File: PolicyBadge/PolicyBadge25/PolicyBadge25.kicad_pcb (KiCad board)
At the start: 2 copper layers, 90.4 x 89.6 mm, 68 parts, among them CN1 PH2.0-2P-LT, J1 Feed Point 915MHz, J2 Feed Point 2.4 GHz, Q1 2N7002, SW1 TA-3525-A1, U1 HS96L03W2C03, U10 YX-SMD5020, U11 IP2312-4V35, U2 MOUDLE-SEEEDUINO-XIAO-ESP32S3, U4 TPS613222ADBVR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

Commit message: Updated PCB routing
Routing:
- net VCC_3V3: track 265.5 -> 284.2 mm
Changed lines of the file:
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@@
-	)
-	(segment
-		(start 119 56.7)
-		(end 139.1 56.7)
-		(width 0.508)
-		(layer "B.Cu")
-		(net 8)
 	)
 	(segment
@@
 	)
 	(segment
+		(start 121.4 69.5)
+		(end 118.9 67)
+		(width 0.508)
+		(layer "B.Cu")
+		(net 8)
+	)
+	(segment
 		(start 150.1 109.7)
 		(end 150.1 104.6)
@@
 	)
 	(segment
-		(start 139.1 56.7)
-		(end 142.2 53.6)
+		(start 142.2 53.1)
+		(end 142.2 66.4)
 		(width 0.508)
 		(layer "B.Cu")
@@
 	)
 	(segment
+		(start 118.9 67)
+		(end 118.9 62.2)
+		(width 0.508)
+		(layer "B.Cu")
+		(net 8)
+	)
+	(segment
 		(start 129.33 76.53)
 		(end 132.5 79.7)
@@
 	)
 	(segment
+		(start 139.1 69.5)
+		(end 121.4 69.5)
+		(width 0.508)
+		(layer "B.Cu")
+		(net 8)
+	)
+	(segment
 		(start 129.33 73.89)
 		(end 129.33 76.53)
@@
 	)
 	(segment
-		(start 142.2 53.6)
-		(end 142.2 53.1)
-		(width 0.508)
-		(layer "B.Cu")
-		(net 8)
-	)
-	(segment
 		(start 158.2 102.4)
 		(end 155.5 102.4)
 		(width 0.254)
+		(layer "B.Cu")
+		(net 8)
+	)
+	(segment
+		(start 142.2 66.4)
+		(end 139.1 69.5)
+		(width 0.508)
 		(layer "B.Cu")
 		(net 8)
@@
 		(min_thickness 0.25)
 		(filled_areas_thickness no)
-		(fill yes
+		(fill
 			(thermal_gap 0.5)
 			(thermal_bridge_width 0.5)
@@
 		(min_thickness 0.25)
 		(filled_areas_thickness no)
-		(fill yes
+		(fill
 			(thermal_gap 0.5)
 			(thermal_bridge_width 0.5)
@@
 		(min_thickness 0.25)
 		(filled_areas_thickness no)
-		(fill yes
+		(fill
 			(thermal_gap 0.5)
 			(thermal_bridge_width 0.5)
@@
 		(min_thickness 0.25)
 		(filled_areas_thickness no)
-		(fill yes
+		(fill
 			(thermal_gap 0.5)
 			(thermal_bridge_width 0.5)
@@
 		(min_thickness 0.25)
 		(filled_areas_thickness no)
-		(fill yes
+		(fill
 			(thermal_gap 0.5)
 			(thermal_bridge_width 0.5)
@@
 		(min_thickness 0.25)
 		(filled_areas_thickness no)
-		(fill yes
+		(fill
 			(thermal_gap 0.5)
 			(thermal_bridge_width 0.5)

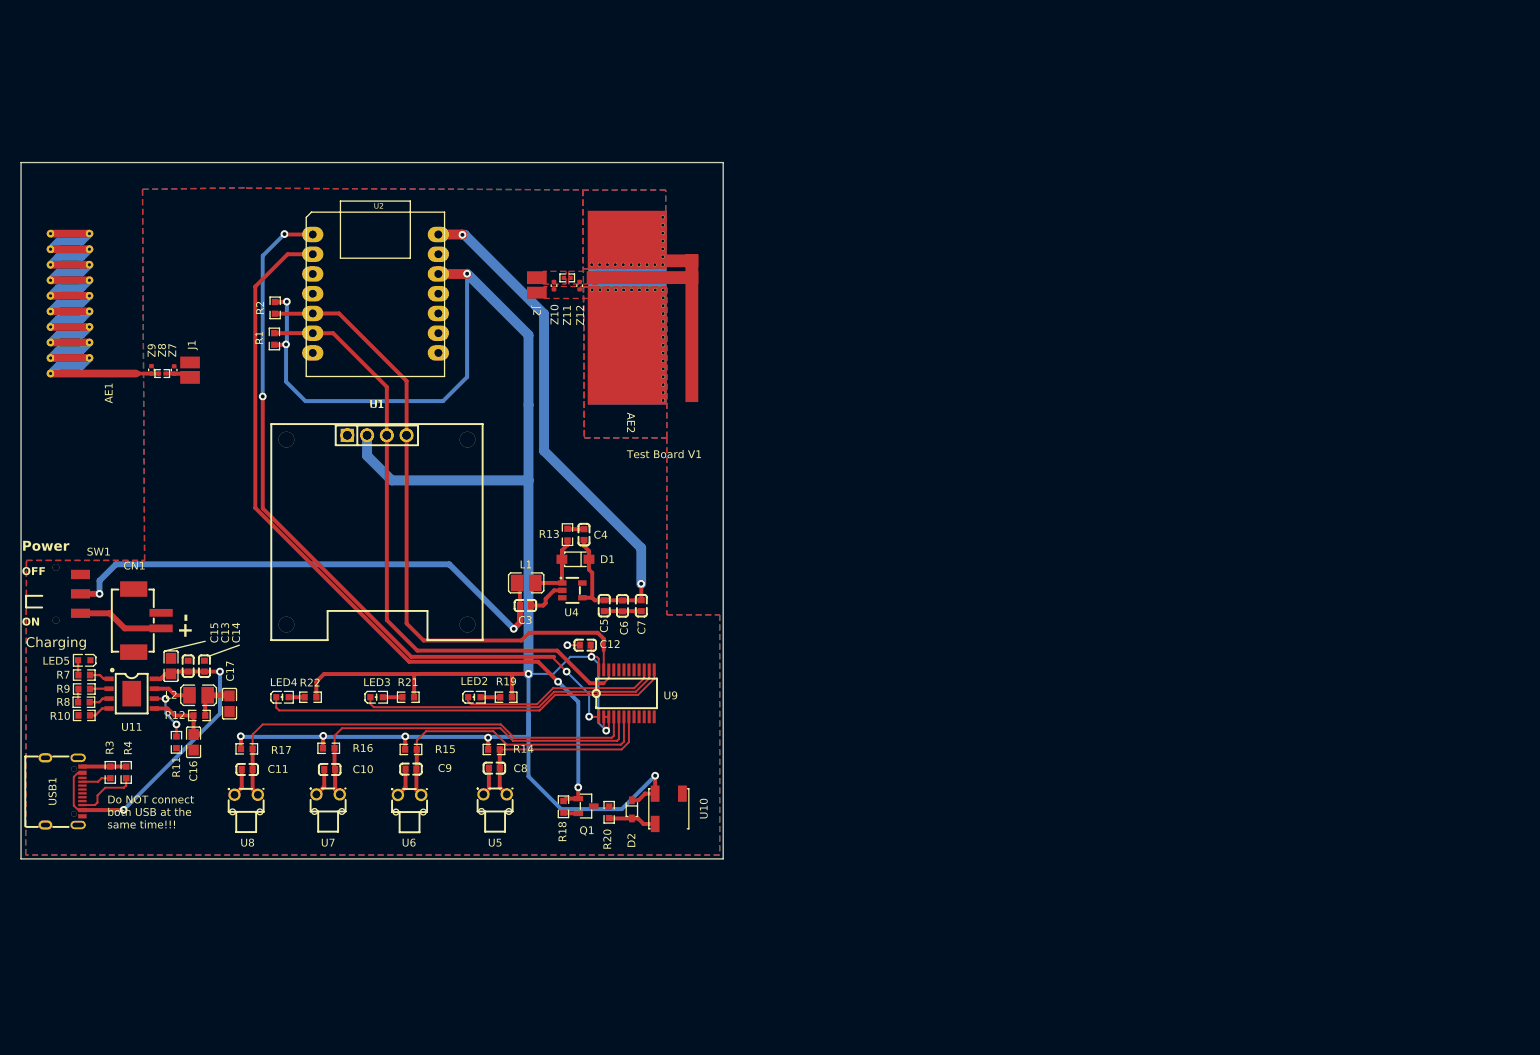
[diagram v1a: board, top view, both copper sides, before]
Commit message: minor updates
imported new switch footprint and schematic symbol. sync'ed the PCB to add R23, R5, R6. annotated.
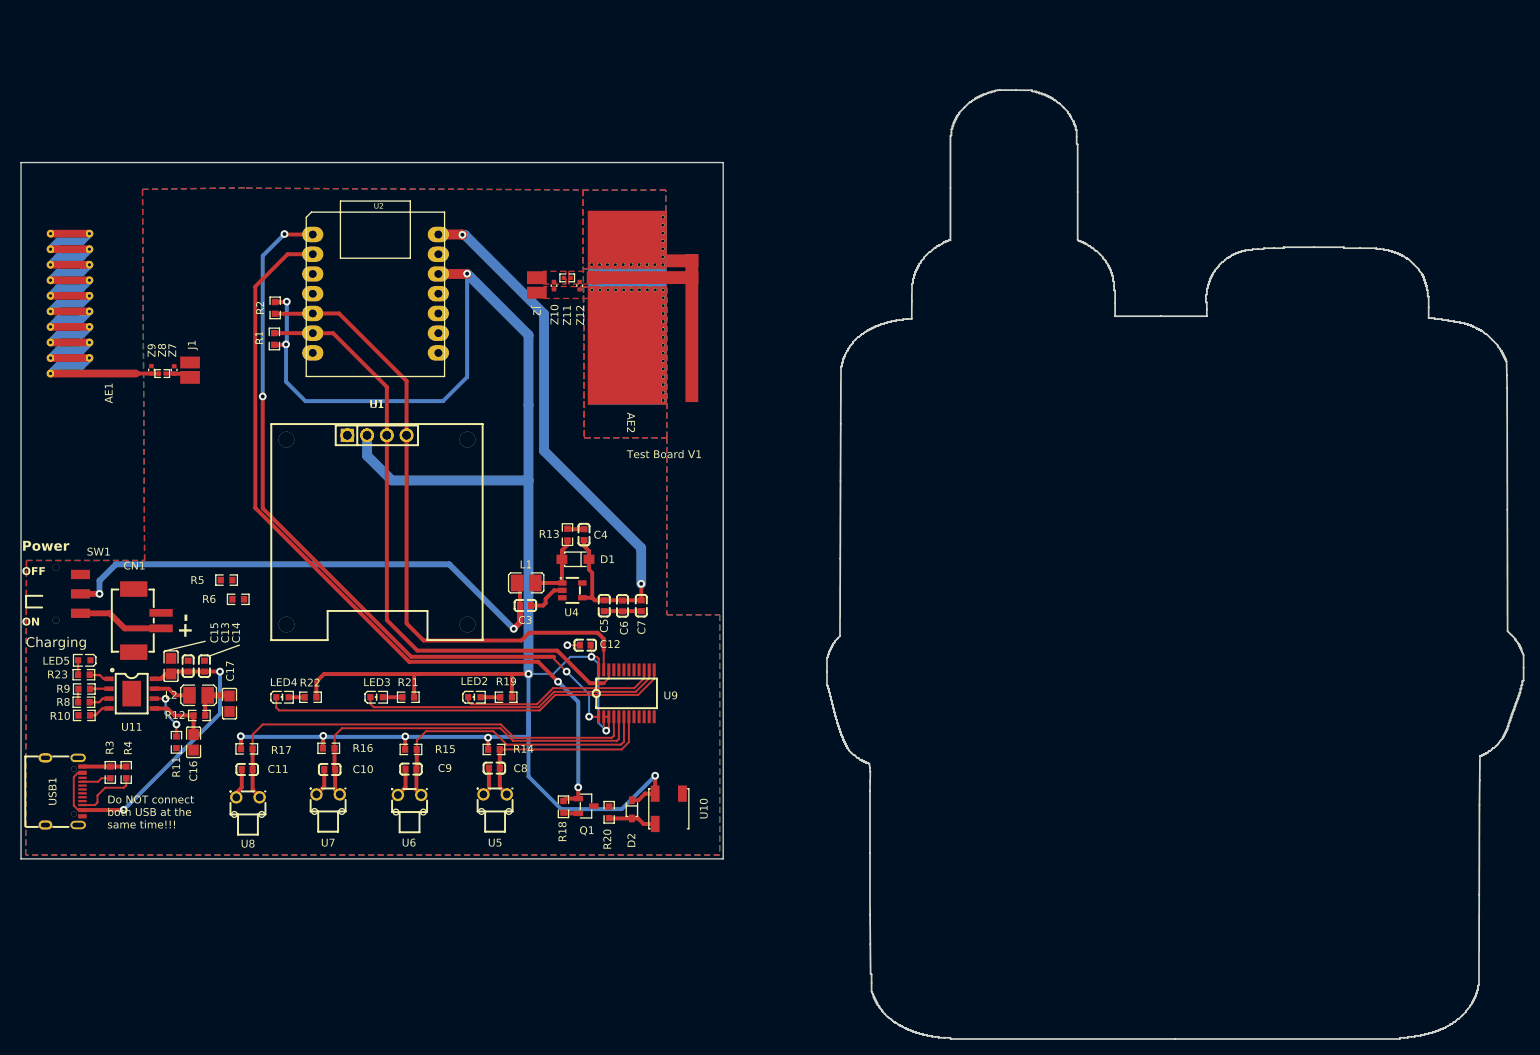
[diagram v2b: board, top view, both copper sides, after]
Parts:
- removed R7: 240Ω, imported:R0603
- added R23: 1KΩ, imported:R0603, F.Cu at (92.9, 104.7)
- added R5: 220kΩ, imported:R0603, F.Cu at (111.2, 92.5)
- added R6: 220kΩ, imported:R0603, F.Cu at (112.8, 95.0)
- moved U8 0.40 mm to (114.0, 120.5)
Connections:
- net /VBATT+ renamed VBATT+
- U2 pad 1: /IO Expander and LED's/IO_INT -> Net-(U2-PA02_A0_D0)
- U2 pad 2: /IO Expander and LED's/BUZZER -> /IO Expander and LED's/IO_INT
- U2 pad 3: unconnected-(U2-PA10_A2_D2-Pad3) -> /IO Expander and LED's/BUZZER
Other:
- board size 90.4 x 89.6 mm -> 193.3 x 122.1 mm

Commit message: battery silk screen + Lanyard
added battery silk screen outline (23mmx34mm is battery, silk screen rectangle is 25x36mm). also added edge cuts for the lanyard holes.
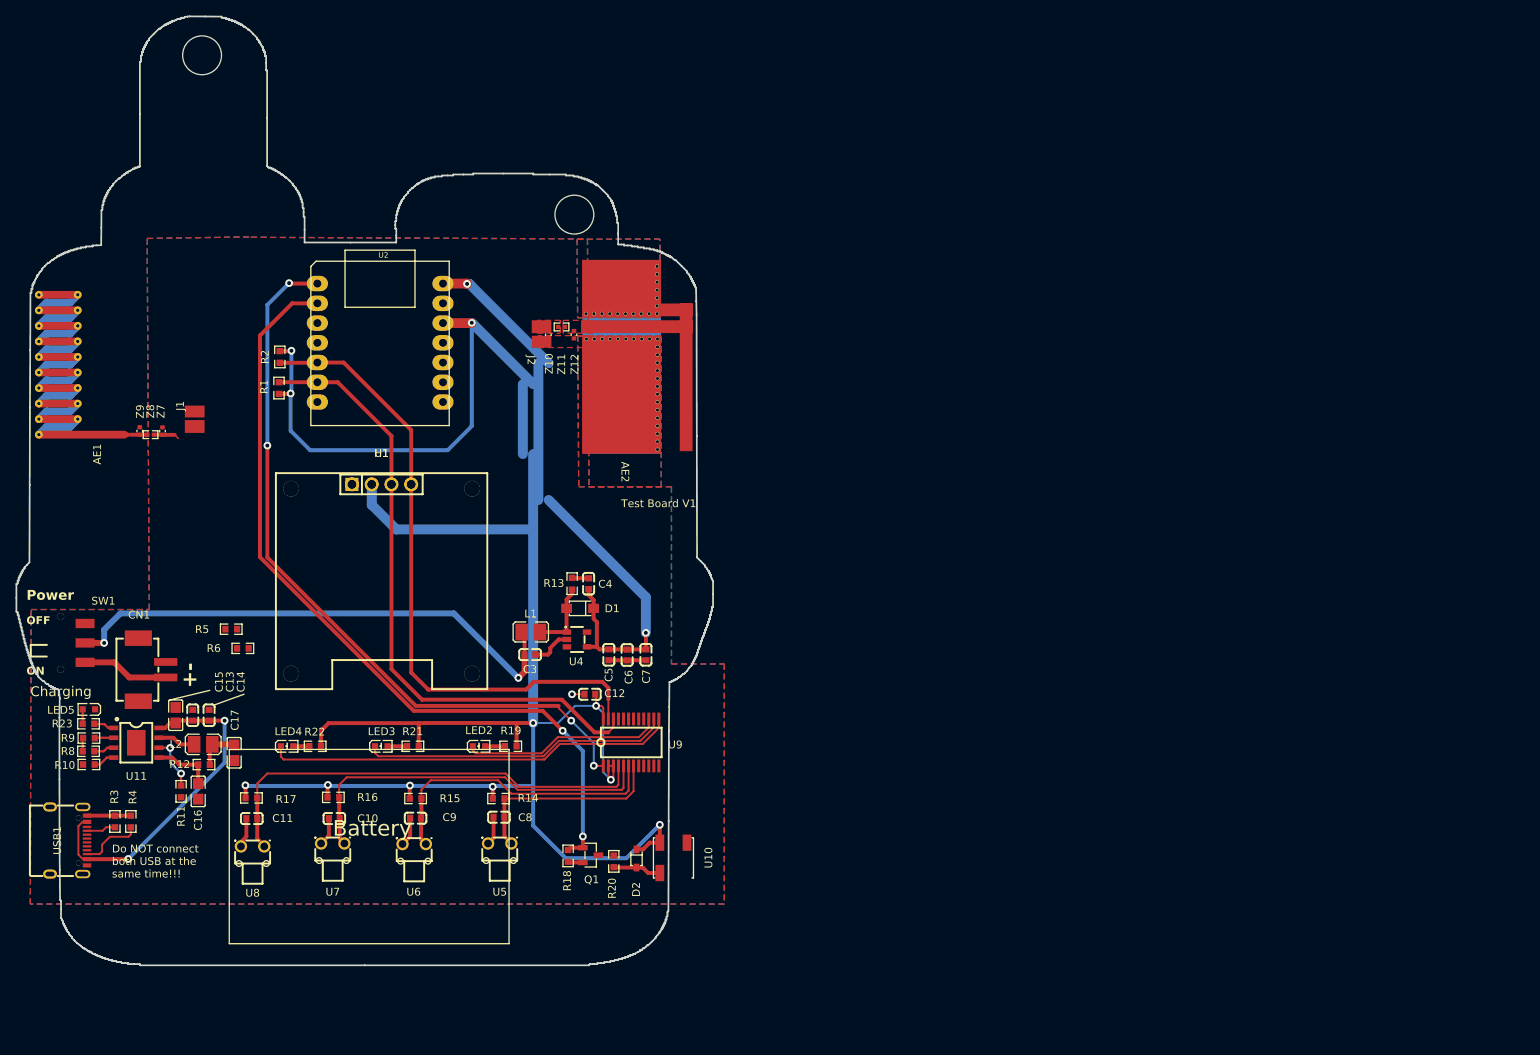
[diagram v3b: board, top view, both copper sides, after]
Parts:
- moved Z9 8.01 mm to (100.1, 73.3)
- moved AE1 8.01 mm to (92.9, 64.8)
- moved Z7 8.01 mm to (103.0, 73.4)
- moved Z8 8.01 mm to (101.5, 73.8)
- moved AE2 6.36 mm to (171.2, 56.9)
- moved Z10 6.36 mm to (152.6, 61.0)
- moved Z11 6.36 mm to (154.3, 60.0)
- moved Z12 6.36 mm to (155.9, 61.0)
- moved C13 6.34 mm to (106.9, 109.9)
- moved C14 6.34 mm to (109.0, 109.9)
- moved C15 6.34 mm to (104.7, 109.9)
- moved C6 6.34 mm to (162.8, 102.2)
- moved CN1 6.34 mm to (101.7, 104.1)
- moved D1 6.34 mm to (156.7, 96.2)
- moved D2 6.34 mm to (164.0, 128.3)
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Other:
- board size 193.3 x 122.1 mm -> 89.6 x 122.1 mm
- board text added: "Battery"

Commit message: removed U5 switch
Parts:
- removed U8: ~, imported:SW-TH_HRO_K2-1109DF-EXXW-XX
